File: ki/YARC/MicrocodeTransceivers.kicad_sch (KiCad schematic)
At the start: 6 parts, among them U66 74HC245, U67 74LS574, U68 74LS574, U69 74HC245, U70 74HC245, U97 74HC00

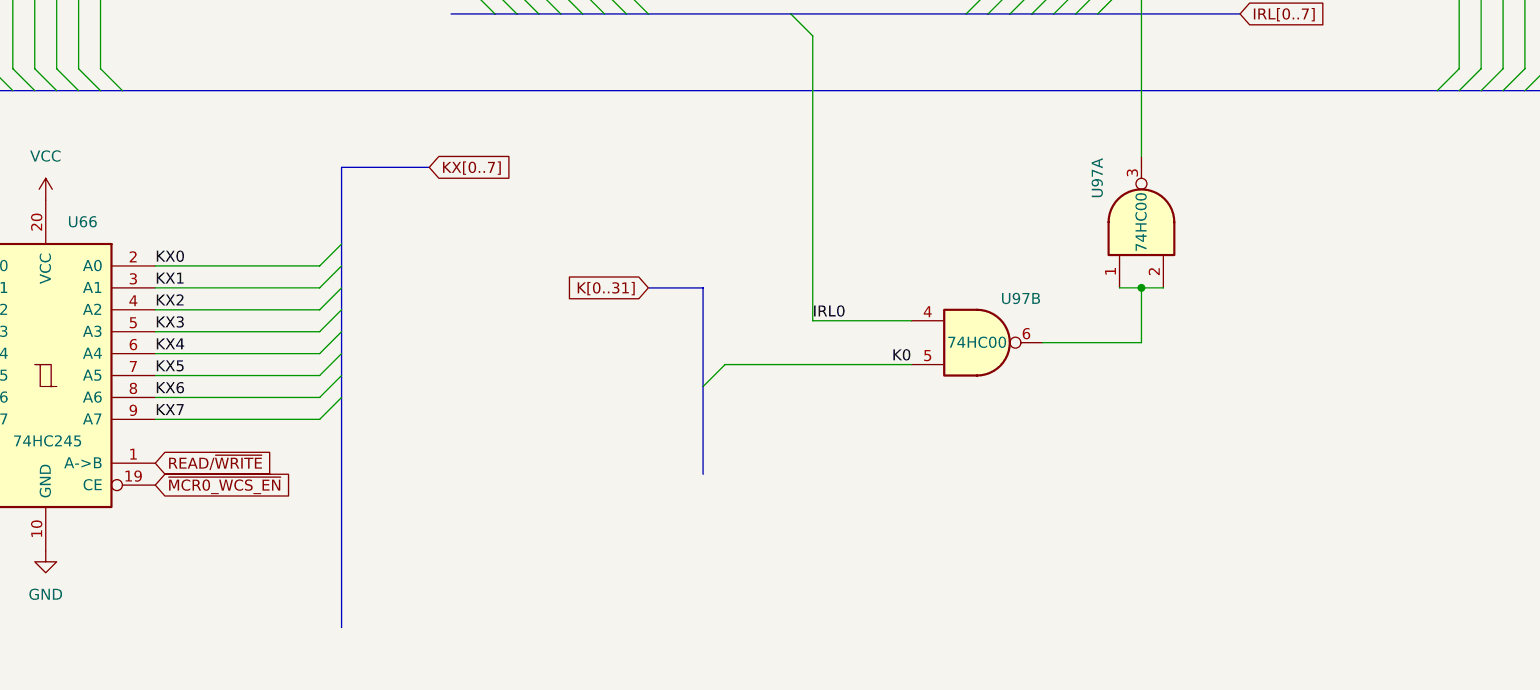
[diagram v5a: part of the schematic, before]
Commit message: Schematic for addressing unit is complete and all ERC violations addressed
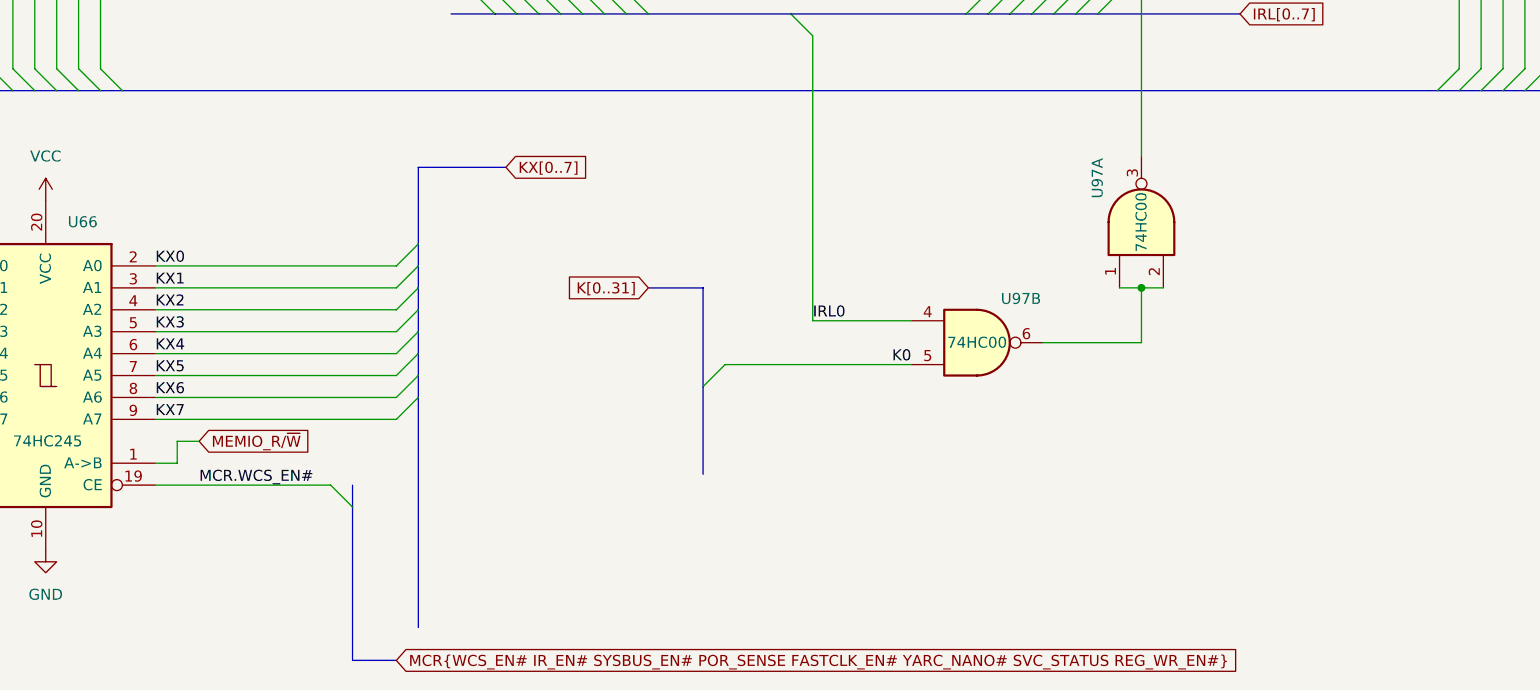
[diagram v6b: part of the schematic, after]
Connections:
- net READ/~{WRITE} renamed MEMIO_R/~{W}
- net ~{MCR0_WCS_EN} renamed MCR.WCS_EN#
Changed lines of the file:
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@@
     (stroke (width 0) (type default))
   )
-  (bus_entry (at 86.36 114.3) (size -2.54 2.54)
+  (bus_entry (at 95.25 114.3) (size -2.54 2.54)
     (stroke (width 0) (type default))
   )
@@
     (stroke (width 0) (type default))
   )
-  (bus_entry (at 86.36 106.68) (size -2.54 2.54)
+  (bus_entry (at 87.63 137.16) (size -2.54 -2.54)
+    (stroke (width 0) (type default))
+  )
+  (bus_entry (at 95.25 106.68) (size -2.54 2.54)
     (stroke (width 0) (type default))
   )
@@
     (stroke (width 0) (type default))
   )
-  (bus_entry (at 86.36 124.46) (size -2.54 2.54)
+  (bus_entry (at 95.25 124.46) (size -2.54 2.54)
     (stroke (width 0) (type default))
   )
@@
     (stroke (width 0) (type default))
   )
-  (bus_entry (at 86.36 116.84) (size -2.54 2.54)
+  (bus_entry (at 95.25 116.84) (size -2.54 2.54)
     (stroke (width 0) (type default))
   )
@@
     (stroke (width 0) (type default))
   )
-  (bus_entry (at 86.36 119.38) (size -2.54 2.54)
+  (bus_entry (at 95.25 119.38) (size -2.54 2.54)
     (stroke (width 0) (type default))
   )
@@
     (stroke (width 0) (type default))
   )
-  (bus_entry (at 86.36 109.22) (size -2.54 2.54)
-    (stroke (width 0) (type default))
-  )
-  (bus_entry (at 86.36 111.76) (size -2.54 2.54)
+  (bus_entry (at 95.25 109.22) (size -2.54 2.54)
+    (stroke (width 0) (type default))
+  )
+  (bus_entry (at 95.25 111.76) (size -2.54 2.54)
     (stroke (width 0) (type default))
   )
@@
     (stroke (width 0) (type default))
   )
-  (bus_entry (at 86.36 121.92) (size -2.54 2.54)
+  (bus_entry (at 95.25 121.92) (size -2.54 2.54)
     (stroke (width 0) (type default))
   )
@@
     (stroke (width 0) (type default))
   )
+  (bus (pts (xy 87.63 134.62) (xy 87.63 137.16))
+    (stroke (width 0) (type default))
+  )
   (bus (pts (xy 218.44 88.9) (xy 220.98 88.9))
     (stroke (width 0) (type default))
@@
     (stroke (width 0) (type default))
   )
-  (bus (pts (xy 86.36 109.22) (xy 86.36 111.76))
-    (stroke (width 0) (type default))
-  )
-  (bus (pts (xy 96.52 97.79) (xy 86.36 97.79))
+  (bus (pts (xy 95.25 109.22) (xy 95.25 111.76))
+    (stroke (width 0) (type default))
+  )
+  (bus (pts (xy 105.41 97.79) (xy 95.25 97.79))
     (stroke (width 0) (type default))
   )
@@
     (stroke (width 0) (type default))
   )
+  (bus (pts (xy 87.63 137.16) (xy 87.63 154.94))
+    (stroke (width 0) (type default))
+  )
   (bus (pts (xy 228.6 88.9) (xy 231.14 88.9))
     (stroke (width 0) (type default))
@@
     (stroke (width 0) (type default))
   )
-  (wire (pts (xy 64.77 127) (xy 83.82 127))
+  (wire (pts (xy 64.77 127) (xy 92.71 127))
     (stroke (width 0) (type default))
   )
@@
     (stroke (width 0) (type default))
   )
-  (wire (pts (xy 64.77 119.38) (xy 83.82 119.38))
-    (stroke (width 0) (type default))
-  )
-  (bus (pts (xy 86.36 116.84) (xy 86.36 119.38))
+  (wire (pts (xy 64.77 119.38) (xy 92.71 119.38))
+    (stroke (width 0) (type default))
+  )
+  (bus (pts (xy 95.25 116.84) (xy 95.25 119.38))
     (stroke (width 0) (type default))
   )
@@
     (stroke (width 0) (type default))
   )
-  (bus (pts (xy 86.36 121.92) (xy 86.36 124.46))
-    (stroke (width 0) (type default))
-  )
-  (wire (pts (xy 64.77 121.92) (xy 83.82 121.92))
+  (bus (pts (xy 95.25 121.92) (xy 95.25 124.46))
+    (stroke (width 0) (type default))
+  )
+  (wire (pts (xy 64.77 121.92) (xy 92.71 121.92))
     (stroke (width 0) (type default))
   )
@@
     (stroke (width 0) (type default))
   )
+  (wire (pts (xy 67.31 129.54) (xy 69.85 129.54))
+    (stroke (width 0) (type default))
+  )
   (bus (pts (xy 179.07 19.05) (xy 181.61 19.05))
     (stroke (width 0) (type default))
@@
     (stroke (width 0) (type default))
   )
-  (bus (pts (xy 86.36 97.79) (xy 86.36 106.68))
+  (bus (pts (xy 95.25 97.79) (xy 95.25 106.68))
     (stroke (width 0) (type default))
   )
@@
     (stroke (width 0) (type default))
   )
-  (wire (pts (xy 64.77 116.84) (xy 83.82 116.84))
+  (wire (pts (xy 64.77 116.84) (xy 92.71 116.84))
+    (stroke (width 0) (type default))
+  )
+  (wire (pts (xy 64.77 132.08) (xy 67.31 132.08))
     (stroke (width 0) (type default))
   )
@@
     (stroke (width 0) (type default))
   )
-  (wire (pts (xy 64.77 109.22) (xy 83.82 109.22))
+  (wire (pts (xy 64.77 109.22) (xy 92.71 109.22))
     (stroke (width 0) (type default))
   )
@@
     (stroke (width 0) (type default))
   )
+  (bus (pts (xy 92.71 154.94) (xy 87.63 154.94))
+    (stroke (width 0) (type default))
+  )
+  (wire (pts (xy 67.31 132.08) (xy 67.31 129.54))
+    (stroke (width 0) (type default))
+  )
   (bus (pts (xy 138.43 80.01) (xy 158.75 80.01))
     (stroke (width 0) (type default))
@@
     (stroke (width 0) (type default))
   )
-  (bus (pts (xy 86.36 106.68) (xy 86.36 109.22))
-    (stroke (width 0) (type default))
-  )
-  (wire (pts (xy 64.77 111.76) (xy 83.82 111.76))
+  (bus (pts (xy 95.25 106.68) (xy 95.25 109.22))
+    (stroke (width 0) (type default))
+  )
+  (wire (pts (xy 64.77 111.76) (xy 92.71 111.76))
     (stroke (width 0) (type default))
   )
@@
     (stroke (width 0) (type default))
   )
-  (bus (pts (xy 86.36 119.38) (xy 86.36 121.92))
+  (bus (pts (xy 95.25 119.38) (xy 95.25 121.92))
     (stroke (width 0) (type default))
   )
@@
     (stroke (width 0) (type default))
   )
-  (wire (pts (xy 64.77 114.3) (xy 83.82 114.3))
+  (wire (pts (xy 64.77 114.3) (xy 92.71 114.3))
     (stroke (width 0) (type default))
   )
@@
     (stroke (width 0) (type default))
   )
-  (bus (pts (xy 86.36 114.3) (xy 86.36 116.84))
+  (bus (pts (xy 95.25 114.3) (xy 95.25 116.84))
     (stroke (width 0) (type default))
   )
@@
     (stroke (width 0) (type default))
   )
-  (wire (pts (xy 64.77 124.46) (xy 83.82 124.46))
+  (wire (pts (xy 64.77 124.46) (xy 92.71 124.46))
     (stroke (width 0) (type default))
   )
@@
     (stroke (width 0) (type default))
   )
-  (bus (pts (xy 86.36 124.46) (xy 86.36 151.13))
+  (bus (pts (xy 95.25 124.46) (xy 95.25 151.13))
     (stroke (width 0) (type default))
   )
@@
     (stroke (width 0) (type default))
   )
-  (bus (pts (xy 86.36 111.76) (xy 86.36 114.3))
+  (bus (pts (xy 95.25 111.76) (xy 95.25 114.3))
     (stroke (width 0) (type default))
   )
@@
     (stroke (width 0) (type default))
   )
+  (wire (pts (xy 64.77 134.62) (xy 85.09 134.62))
+    (stroke (width 0) (type default))
+  )
   (wire (pts (xy 50.8 21.59) (xy 50.8 40.64))
     (stroke (width 0) (type default))
@@
     (effects (font (size 1.27 1.27)) (justify right bottom))
   )
+  (label "MCR.WCS_EN#" (at 69.85 134.62 0) (fields_autoplaced)
+    (effects (font (size 1.27 1.27)) (justify left bottom))
+  )
   (label "IRL7" (at 119.38 66.04 270) (fields_autoplaced)
     (effects (font (size 1.27 1.27)) (justify right bottom))
@@
     (effects (font (size 1.27 1.27)) (justify right bottom))
   )
-  (global_label "~{MCR0_WCS_EN}" (shape input) (at 64.77 134.62 0) (fields_autoplaced)
+  (global_label "MCR{WCS_EN# IR_EN# SYSBUS_EN# POR_SENSE FASTCLK_EN# YARC_NANO# SVC_STATUS REG_WR_EN#}" (shape input)
+    (at 92.71 154.94 0) (fields_autoplaced)
     (effects (font (size 1.27 1.27)) (justify left))
-    (property "Intersheetrefs" "${INTERSHEET_REFS}" (at 81.3017 134.62 0)
-      (effects (font (size 1.27 1.27)) (justify left) hide)
-    )
-  )
-  (global_label "READ{slash}~{WRITE}" (shape input) (at 64.77 132.08 0) (fields_autoplaced)
-    (effects (font (size 1.27 1.27)) (justify left))
-    (property "Intersheetrefs" "${INTERSHEET_REFS}" (at 78.7341 132.0006 0)
+    (property "Intersheetrefs" "${INTERSHEET_REFS}" (at 194.3919 154.94 0)
       (effects (font (size 1.27 1.27)) (justify left) hide)
     )
@@
     )
   )
-  (global_label "KX[0..7]" (shape input) (at 96.52 97.79 0) (fields_autoplaced)
+  (global_label "KX[0..7]" (shape input) (at 105.41 97.79 0) (fields_autoplaced)
     (effects (font (size 1.27 1.27)) (justify left))
-    (property "Intersheetrefs" "${INTERSHEET_REFS}" (at 107.3067 97.79 0)
+    (property "Intersheetrefs" "${INTERSHEET_REFS}" (at 116.1967 97.79 0)
       (effects (font (size 1.27 1.27)) (justify left) hide)
     )
@@
     )
   )
+  (global_label "MEMIO_R{slash}~{W}" (shape input) (at 69.85 129.54 0) (fields_autoplaced)
+    (effects (font (size 1.27 1.27)) (justify left))
+    (property "Intersheetrefs" "${INTERSHEET_REFS}" (at 83.8418 129.54 0)
+      (effects (font (size 1.27 1.27)) (justify left) hide)
+    )
+  )
